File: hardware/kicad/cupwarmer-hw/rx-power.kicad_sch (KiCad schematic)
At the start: 39 parts, among them J1 I2C Service, U1 STWLC38JRM

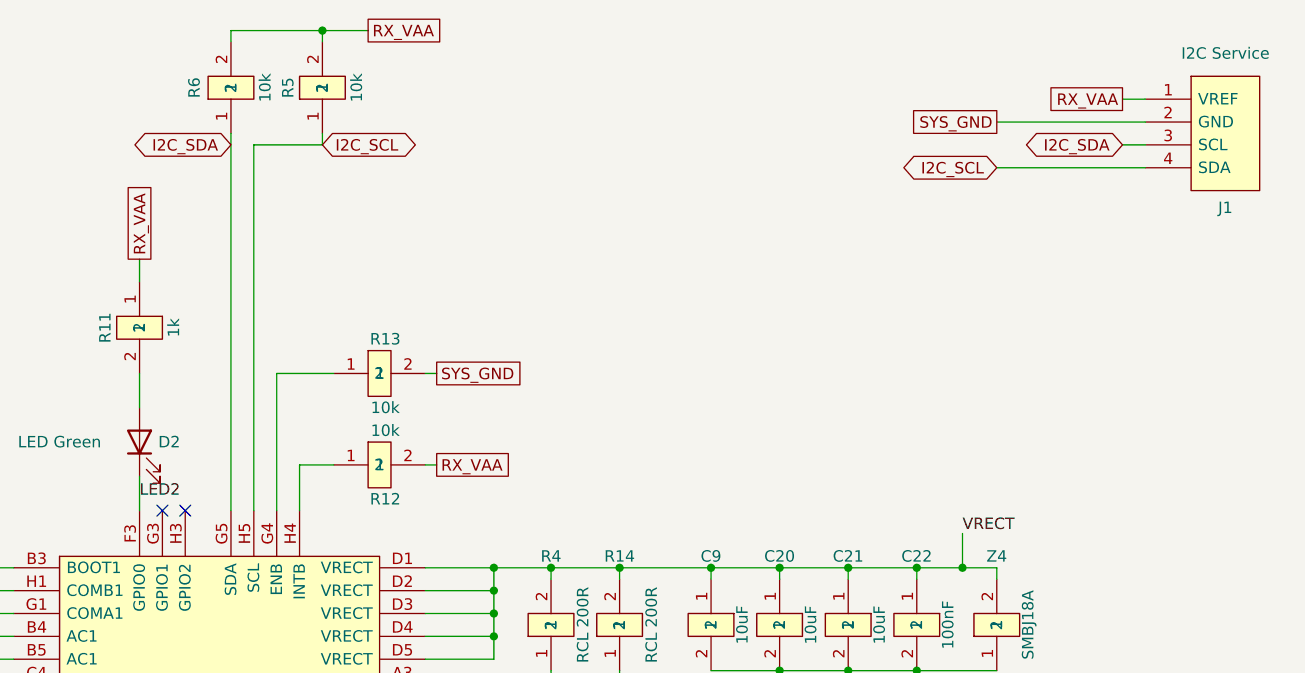
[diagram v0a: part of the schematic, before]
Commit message: Apply pre-order dual review fixes
Pre-order schematic/PCB review decisions from
docs/plans/20260517-pre-order-review-issues.md:

- R1 15k -> 12k (UNI-ROYAL C22790): Q1 VGS_normal 4.8V -> 5.45V
  with clamp-time VGS=11.09V still inside AO3400 +/-12V (margin 0.91V)
- D3 = B5819W Schottky (SOD-123, C8598): heater flyback / freewheel
  between Q1.drain (anode) and VOUT_12V (cathode). New DIODE_2 symbol
  in cupwarmer.kicad_sym; D3 placed near H1 at (100, 126) F.Cu.
  Zone connection tracks still to be routed in KiCad GUI
- R11 1k -> 100R (UNI-ROYAL C22775): GPIO0 LED Vf margin and
  reliable lighting at I ~= 3mA; document NVM-write-first bring-up
  procedure to avoid GPIO0 dragging during high-Z input default
- R15/R16 = 100R 0603 (UNI-ROYAL C22775): I2C SDA/SCL series
  protection at U1 side of J1 service header; substitutes for ESD
  diodes via bring-up ESD strap operating practice
- design-notes: document F1 implemented on heater assembly side
  (not on PCB), 1.0A continuous / 1.5A short bring-up shunt limit
  (5A evaluation explicitly forbidden), and rationale for above
  component changes

Co-Authored-By: Claude Opus 4.7 (1M context) <noreply@anthropic.com>
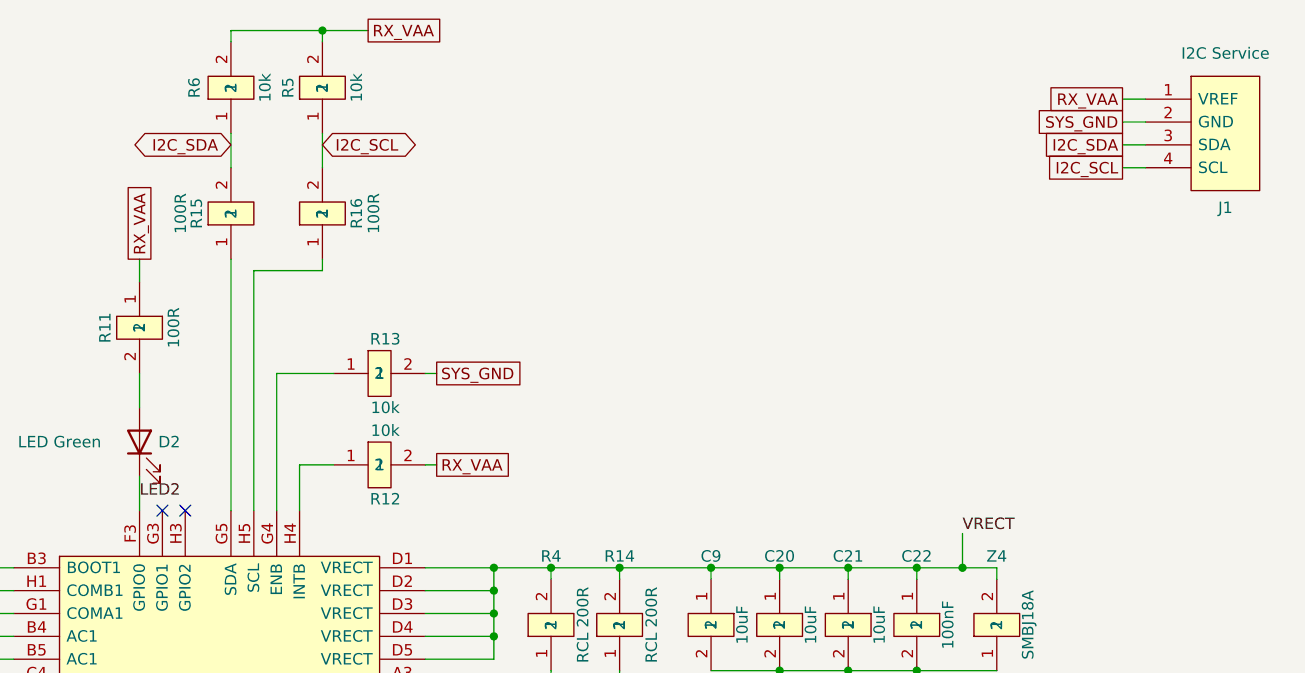
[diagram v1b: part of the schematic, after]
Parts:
- added R15, R16: 100R, Resistor_SMD:R_0603_1608Metric, symbol cupwarmer:PASSIVE_2
- R11: value 1k -> 100R; LCSC C21190 -> C22775; MPN 0603WAF1001T5E -> 0603WAF1000T5E
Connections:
- net I2C_SCL: now also R16.2; no longer U1.H5 (SCL)
- net I2C_SDA: now also R15.2; no longer U1.G5 (SDA)
- new net: R16.1, U1.H5 (SCL)
- new net: R15.1, U1.G5 (SDA)

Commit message: Swap C11/C13/C18/C19 to Murata GRM1885C1H103JA01D; regen fab outputs
YAGEO CC0603JRNPO9BN103 (C389113) is low-stock on JLCPCB (~1.2k, Extended).
Swap the four 10nF/50V C0G caps to Murata GRM1885C1H103JA01D (C85973,
in-stock) in rx-power.kicad_sch and both BOMs. Same value/footprint/
dielectric/tolerance — electrically equivalent drop-in.

Also regenerate gerbers, drill files, and the JLCPCB CPL from the current
PCB.

Co-Authored-By: Claude Opus 4.8 (1M context) <noreply@anthropic.com>
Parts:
- C11, C13, C18, C19: LCSC C389113 -> C85973; MPN CC0603JRNPO9BN103 -> GRM1885C1H103JA01D; Manufacturer YAGEO -> Murata Electronics
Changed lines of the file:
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@@
 			)
 		)
-		(property "Manufacturer" "YAGEO"
-			(at 0 0 0)
-			(hide yes)
-			(show_name no)
-			(do_not_autoplace no)
-			(effects
-				(font
-					(size 1.27 1.27)
-				)
-			)
-		)
-		(property "LCSC" "C389113"
-			(at 0 0 0)
-			(hide yes)
-			(show_name no)
-			(do_not_autoplace no)
-			(effects
-				(font
-					(size 1.27 1.27)
-				)
-			)
-		)
-		(property "MPN" "CC0603JRNPO9BN103"
+		(property "Manufacturer" "Murata Electronics"
+			(at 0 0 0)
+			(hide yes)
+			(show_name no)
+			(do_not_autoplace no)
+			(effects
+				(font
+					(size 1.27 1.27)
+				)
+			)
+		)
+		(property "LCSC" "C85973"
+			(at 0 0 0)
+			(hide yes)
+			(show_name no)
+			(do_not_autoplace no)
+			(effects
+				(font
+					(size 1.27 1.27)
+				)
+			)
+		)
+		(property "MPN" "GRM1885C1H103JA01D"
 			(at 0 0 0)
 			(hide yes)
@@
 			)
 		)
-		(property "Manufacturer" "YAGEO"
-			(at 0 0 0)
-			(hide yes)
-			(show_name no)
-			(do_not_autoplace no)
-			(effects
-				(font
-					(size 1.27 1.27)
-				)
-			)
-		)
-		(property "LCSC" "C389113"
-			(at 0 0 0)
-			(hide yes)
-			(show_name no)
-			(do_not_autoplace no)
-			(effects
-				(font
-					(size 1.27 1.27)
-				)
-			)
-		)
-		(property "MPN" "CC0603JRNPO9BN103"
+		(property "Manufacturer" "Murata Electronics"
+			(at 0 0 0)
+			(hide yes)
+			(show_name no)
+			(do_not_autoplace no)
+			(effects
+				(font
+					(size 1.27 1.27)
+				)
+			)
+		)
+		(property "LCSC" "C85973"
+			(at 0 0 0)
+			(hide yes)
+			(show_name no)
+			(do_not_autoplace no)
+			(effects
+				(font
+					(size 1.27 1.27)
+				)
+			)
+		)
+		(property "MPN" "GRM1885C1H103JA01D"
 			(at 0 0 0)
 			(hide yes)
@@
 			)
 		)
-		(property "Manufacturer" "YAGEO"
-			(at 0 0 0)
-			(hide yes)
-			(show_name no)
-			(do_not_autoplace no)
-			(effects
-				(font
-					(size 1.27 1.27)
-				)
-			)
-		)
-		(property "LCSC" "C389113"
-			(at 0 0 0)
-			(hide yes)
-			(show_name no)
-			(do_not_autoplace no)
-			(effects
-				(font
-					(size 1.27 1.27)
-				)
-			)
-		)
-		(property "MPN" "CC0603JRNPO9BN103"
+		(property "Manufacturer" "Murata Electronics"
+			(at 0 0 0)
+			(hide yes)
+			(show_name no)
+			(do_not_autoplace no)
+			(effects
+				(font
+					(size 1.27 1.27)
+				)
+			)
+		)
+		(property "LCSC" "C85973"
+			(at 0 0 0)
+			(hide yes)
+			(show_name no)
+			(do_not_autoplace no)
+			(effects
+				(font
+					(size 1.27 1.27)
+				)
+			)
+		)
+		(property "MPN" "GRM1885C1H103JA01D"
 			(at 0 0 0)
 			(hide yes)
@@
 			)
 		)
-		(property "Manufacturer" "YAGEO"
-			(at 0 0 0)
-			(hide yes)
-			(show_name no)
-			(do_not_autoplace no)
-			(effects
-				(font
-					(size 1.27 1.27)
-				)
-			)
-		)
-		(property "LCSC" "C389113"
-			(at 0 0 0)
-			(hide yes)
-			(show_name no)
-			(do_not_autoplace no)
-			(effects
-				(font
-					(size 1.27 1.27)
-				)
-			)
-		)
-		(property "MPN" "CC0603JRNPO9BN103"
-			(at 0 0 0)
-			(hide yes)
+		(property "Manufacturer" "Murata Electronics"
+			(at 0 0 0)
+			(hide yes)
+			(show_name no)
+			(do_not_autoplace no)
+			(effects
+				(font
+					(size 1.27 1.27)
+				)
+			)
+		)
+		(property "LCSC" "C85973"
+			(at 0 0 0)
+			(hide yes)
+			(show_name no)
+			(do_not_autoplace no)
+			(effects
+				(font
+					(size 1.27 1.27)
+				)
+			)
+		)
+		(property "MPN" "GRM1885C1H103JA01D"
+			(at 0 0 0)
+			(hide yes)

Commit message: Fix reversed TVS polarity (Z1/Z3/Z4) and convert TVS to zener symbols
Z1-Z4 are unidirectional TVS (SMF13A/SMF13A/SMBJ15A/SMBJ18A) that were
drawn with a generic non-polarized symbol (cupwarmer:PASSIVE_2), hiding a
polarity error: Z1, Z3, Z4 had cathode->GND, anode->positive node (would
forward-conduct and effectively short AC1/VOUT_12V/VRECT). Only Z2 was
correct.

- Re-type Z1-Z4 to Device:D_Zener so polarity is visible; add 1.27mm
  collinear stub wires to bridge the D_Zener pin-tip pitch (3.81 vs
  PASSIVE_2's 5.08mm). Embedded lib_symbols updated.
- Rotate Z1/Z3/Z4 180 deg so cathode (pin1/K) faces the protected node:
  Z1->AC1, Z2->AC2, Z3->VOUT_12V, Z4->VRECT; anode->SYS_GND for all.
- PCB: rotate Z1/Z3/Z4 footprints 180 deg and swap their pad nets to match.

Verified: ERC unchanged (0 errors), kicad-cli DRC 0 unconnected / 0 shorts.

Known follow-ups: D_SMB (Z3/Z4) footprints show lib_footprint_mismatch and
silk cathode bar on the wrong side (pre-existing); to be normalized via
re-sync. CPL/gerbers and bom.csv (C18/C19, Z3/Z4 descriptions) still stale.

Co-Authored-By: Claude Opus 4.8 (1M context) <noreply@anthropic.com>
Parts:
- Z1, Z2, Z3, Z4: symbol cupwarmer:PASSIVE_2 -> Device:D_Zener
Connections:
- net AC1: now also Z1.1 (K); no longer Z1.2
- net SYS_GND: now also Z1.2 (A), Z3.2 (A), Z4.2 (A); no longer Z1.1, Z3.1, Z4.1
- net VOUT_12V: now also Z3.1 (K); no longer Z3.2
- net VRECT: now also Z4.1 (K); no longer Z4.2
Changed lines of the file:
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@@
 		)
 	)
+	(wire
+		(pts
+			(xy 72.39 123.19) (xy 72.39 124.46)
+		)
+		(stroke
+			(width 0)
+			(type default)
+		)
+	)
+	(wire
+		(pts
+			(xy 72.39 115.57) (xy 72.39 114.3)
+		)
+		(stroke
+			(width 0)
+			(type default)
+		)
+	)
+	(wire
+		(pts
+			(xy 66.04 115.57) (xy 66.04 114.3)
+		)
+		(stroke
+			(width 0)
+			(type default)
+		)
+	)
+	(wire
+		(pts
+			(xy 66.04 123.19) (xy 66.04 124.46)
+		)
+		(stroke
+			(width 0)
+			(type default)
+		)
+	)
+	(wire
+		(pts
+			(xy 220.98 116.84) (xy 220.98 118.11)
+		)
+		(stroke
+			(width 0)
+			(type default)
+		)
+	)
+	(wire
+		(pts
+			(xy 220.98 109.22) (xy 220.98 107.95)
+		)
+		(stroke
+			(width 0)
+			(type default)
+		)
+	)
+	(wire
+		(pts
+			(xy 236.22 97.79) (xy 236.22 99.06)
+		)
+		(stroke
+			(width 0)
+			(type default)
+		)
+	)
+	(wire
+		(pts
+			(xy 236.22 90.17) (xy 236.22 88.9)
+		)
+		(stroke
+			(width 0)
+			(type default)
+		)
+	)
 	(label "COMB2"
 		(at 116.84 118.11 0)
@@
 	)
 	(symbol
-		(lib_id "cupwarmer:PASSIVE_2")
-		(at 72.39 119.38 90)
+		(lib_id "Device:D_Zener")
+		(at 72.39 119.38 270)
 		(unit 1)
 		(body_style 1)
@@
 		(dnp no)
 		(property "Reference" "Z1"
-			(at 78.74 119.38 0)
+			(at 78.74 119.38 180)
 			(show_name no)
 			(do_not_autoplace no)
@@
 		)
 		(property "Value" "SMF13A Z1"
-			(at 76 119.38 0)
+			(at 76 119.38 180)
 			(show_name no)
 			(do_not_autoplace no)
@@
 		)
 		(property "Footprint" "Diode_SMD:D_SOD-123F"
-			(at 72.39 119.38 0)
+			(at 72.39 119.38 180)
 			(hide yes)
 			(show_name no)
@@
 		)
 		(property "Datasheet" "~"
-			(at 72.39 119.38 0)
+			(at 72.39 119.38 180)
 			(hide yes)
 			(show_name no)
@@
 		)
 		(property "Description" "AC1 ESD clamp TVS (uni-directional)"
-			(at 72.39 119.38 0)
+			(at 72.39 119.38 180)
 			(hide yes)
 			(show_name no)
@@
 	)
 	(symbol
-		(lib_id "cupwarmer:PASSIVE_2")
+		(lib_id "Device:D_Zener")
 		(at 66.04 119.38 270)
 		(unit 1)
@@
 	)
 	(symbol
-		(lib_id "cupwarmer:PASSIVE_2")
-		(at 220.98 113.03 90)
+		(lib_id "Device:D_Zener")
+		(at 220.98 113.03 270)
 		(unit 1)
 		(body_style 1)
@@
 		(dnp no)
 		(property "Reference" "Z3"
-			(at 220.98 120.65 90)
+			(at 220.98 120.65 270)
 			(show_name no)
 			(do_not_autoplace no)
@@
 		)
 		(property "Value" "SMBJ15A"
-			(at 224.536 113.03 0)
+			(at 224.536 113.03 180)
 			(show_name no)
 			(do_not_autoplace no)
@@
 		)
 		(property "Footprint" "Diode_SMD:D_SMB"
-			(at 220.98 113.03 90)
+			(at 220.98 113.03 270)
 			(hide yes)
 			(show_name no)
@@
 		)
 		(property "Datasheet" "/Users/mash/Downloads/SMBJ15A.pdf"
-			(at 220.98 113.03 90)
+			(at 220.98 113.03 270)
 			(hide yes)
 			(show_name no)
@@
 		)
 		(property "Description" "VOUT transient clamp TVS (pin2 cathode to VOUT, pin1 anode to GND)"
-			(at 220.98 113.03 90)
+			(at 220.98 113.03 270)
 			(hide yes)
 			(show_name no)
@@
 	)
 	(symbol
-		(lib_id "cupwarmer:PASSIVE_2")
-		(at 236.22 93.98 90)
+		(lib_id "Device:D_Zener")
+		(at 236.22 93.98 270)
 		(unit 1)
 		(body_style 1)
@@
 		(dnp no)
 		(property "Reference" "Z4"
-			(at 236.22 86.36 90)
+			(at 236.22 86.36 270)
 			(show_name no)
 			(do_not_autoplace no)
@@
 		)
 		(property "Value" "SMBJ18A"
-			(at 239.7 93.98 0)
+			(at 239.7 93.98 180)
 			(show_name no)
 			(do_not_autoplace no)
@@
 		)
 		(property "Footprint" "Diode_SMD:D_SMB"
-			(at 236.22 93.98 90)
+			(at 236.22 93.98 270)
 			(hide yes)
 			(show_name no)
@@
 		)
 		(property "Datasheet" "~"
-			(at 236.22 93.98 90)
+			(at 236.22 93.98 270)
 			(hide yes)
 			(show_name no)
@@
 		)
 		(property "Description" "VRECT OVP TVS clamp (~20V breakdown, pin2 cathode to VRECT, pin1 anode to GND)"
-			(at 236.22 93.98 90)
+			(at 236.22 93.98 270)
 			(hide yes)
 			(show_name no)
